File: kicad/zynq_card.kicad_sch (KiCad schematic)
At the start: 0 parts

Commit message: Phase 2: sheet 6 (SoC config): MIO banks, bank 0, boot straps, JTAG
- tools/sheets/06_soc_config.py: U20 units 6/7 (MIO banks 500/501, 1.8 V)
  with every used MIO as a sheet port, boot straps R601-R607 (QSPI boot,
  JTAG cascaded, PLLs on, VMODE 1.8/1.8), PS_POR_B/PS_SRST_B pull-ups,
  PS_MIO_VREF divider; unit 1 (bank 0 at 1.8 V) tied off as on juliancoy,
  R9/R10 kept as block parts, DONE 330R, RSVDGND open (E8)
- J1 (1x5, 3.3 V for FTDI mini-modules) through U601 SN74AVC4T774RSVR,
  the Agilex 3 card's JTAG shifter circuit
- check_block_netlist.py covers sheet 6: on units 1/6/7 only rail/GND balls
  and balls on block-part nets are compared; E3/E7/E8 expected differences;
  J-refs are never block parts (101 parts, 583 pads, 0 failures)
- gen_symbols: SN74AVC4T774 (RSV) box, Conn_01x05; _common: attach(side=),
  pull_r(top=)
- REUSE_LOG E8 and E5/E6 commit refs; ZYNQ_PCB_NOTES JTAG/RSVDGND and the
  UART translator note (needs per-bit direction); STATUS updated

Co-Authored-By: Claude Opus 5.5 <noreply@anthropic.com>
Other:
- sheet 06 soc_config ports: added emmc_rst_n, eth_int_n, eth_rst_n, i2c_scl, i2c_sda, mdc, mdio, ps_clk, ps_por_n, qspi_cs_n, qspi_io0, qspi_io1, qspi_io2, qspi_io3, qspi_sclk, rgmii_rx_ctl, rgmii_rxc, rgmii_rxd0, rgmii_rxd1, rgmii_rxd2, rgmii_rxd3, rgmii_tx_ctl, rgmii_txc, rgmii_txd0, rgmii_txd1, rgmii_txd2, rgmii_txd3, sd_clk, sd_cmd, sd_dat0, sd_dat1, sd_dat2, sd_dat3, uart_rx, uart_tx; removed none

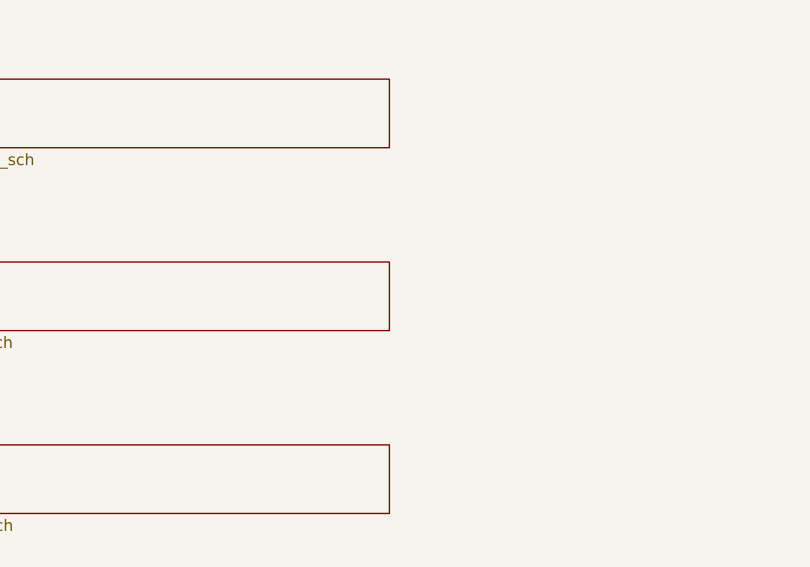
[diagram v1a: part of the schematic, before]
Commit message: Phase 2: sheet 7 (clocks): 33.333 MHz PS_CLK oscillator
- tools/sheets/07_clocks.py: Y701 YXC OT322533.3333MJBA4SL (C2831392,
  1.8 V CMOS, 3225) with the Agilex 3 card's oscillator circuit: EN tied
  to VDD, FB701 BLM18PG121SN1D + C701 470n supply filter, R701 33R
  source-series to the ps_clk port (U20 F7)
- gen_symbols: Oscillator:ASE-xxxMHz
- STATUS updated; REUSE_LOG E8 commit ref

Co-Authored-By: Claude Opus 5.5 <noreply@anthropic.com>
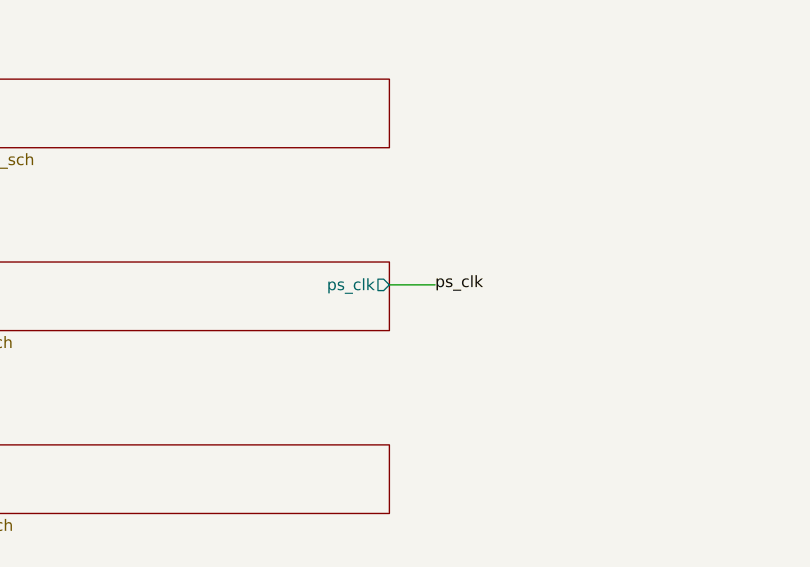
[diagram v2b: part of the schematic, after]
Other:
- sheet 07 clocks ports: added ps_clk; removed none
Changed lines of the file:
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@@
+		)
+	)
+	(label "ps_clk"
+		(at 363.22 53.34 0)
+		(effects
+			(font
+				(size 1.27 1.27)
+			)
+			(justify left)
+		)
+	)
+	(wire
+		(pts
+			(xy 358.14 53.34) (xy 363.22 53.34)
+		)
+		(stroke
+			(width 0)
+			(type default)
 		)
 	)
@@
 			)
 		)
+		(pin "ps_clk" output
+			(at 358.14 53.34 0)
+			(effects
+				(font
+					(size 1.27 1.27)
+				)
+				(justify right)
+			)
+		)

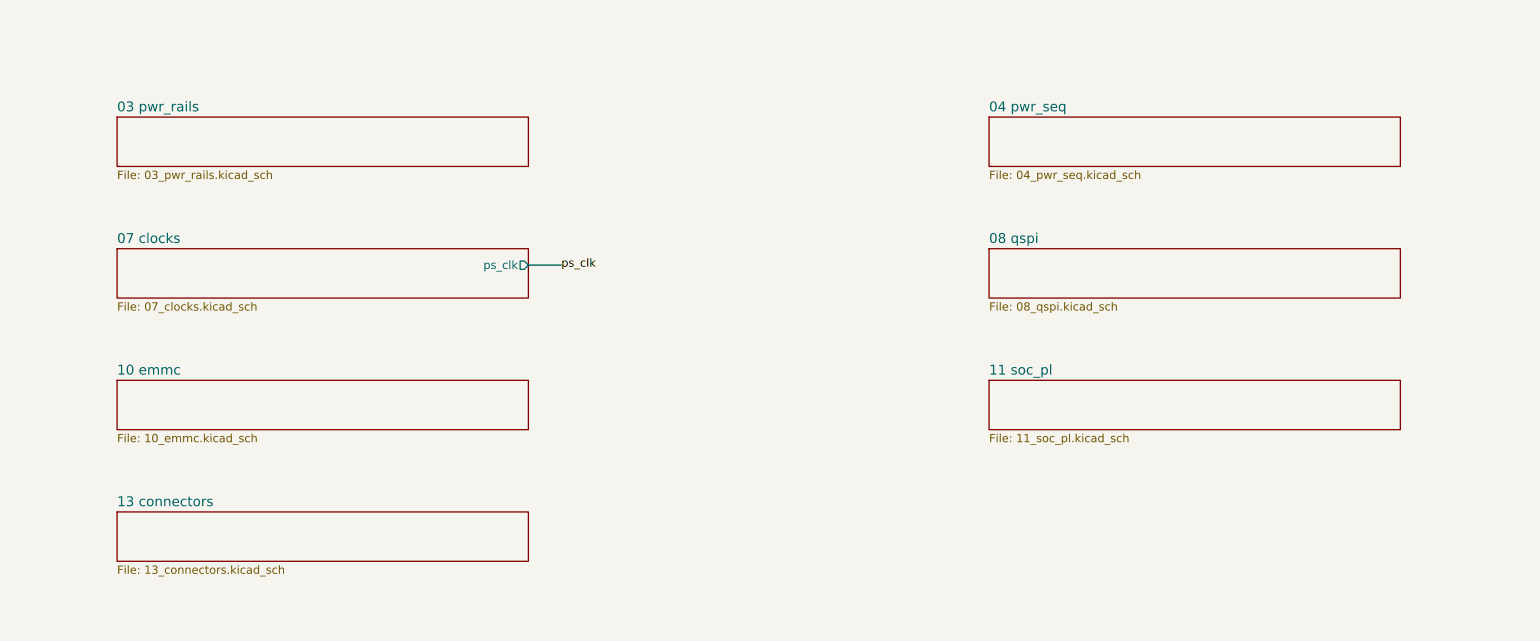
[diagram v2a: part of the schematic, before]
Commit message: Phase 2: sheets 2-4 (power input, rails, sequencing + PS_POR_B supervisor)
Sheet 2: J6 (baseboard J12) to 5V0/GND with PWR_FLAGs and the Ti135 input bulk.
Sheet 3: 4 x TLV62585 (1V0, 1V8, 3V3, 1V35) from the Ti135 cell (_power.py) and
the NCP163 3V3_analog LDO.
Sheet 4: enable chain 1V0 -> 1V8 -> 3V3 + 1V35 -> DDR3_VTT_EN (wired PG AND)
and a TPS3808G01 onto ps_por_n: SENSE on 1V0 (0.895 V), CT = VDD (300 ms),
which keeps PS_POR_B release outside every DS187 Table 23 lockdown window.
Closes the lockdown-window [verify] item. ERC: rails driven; block check 0 failures.

Co-Authored-By: Claude Opus 5.5 <noreply@anthropic.com>
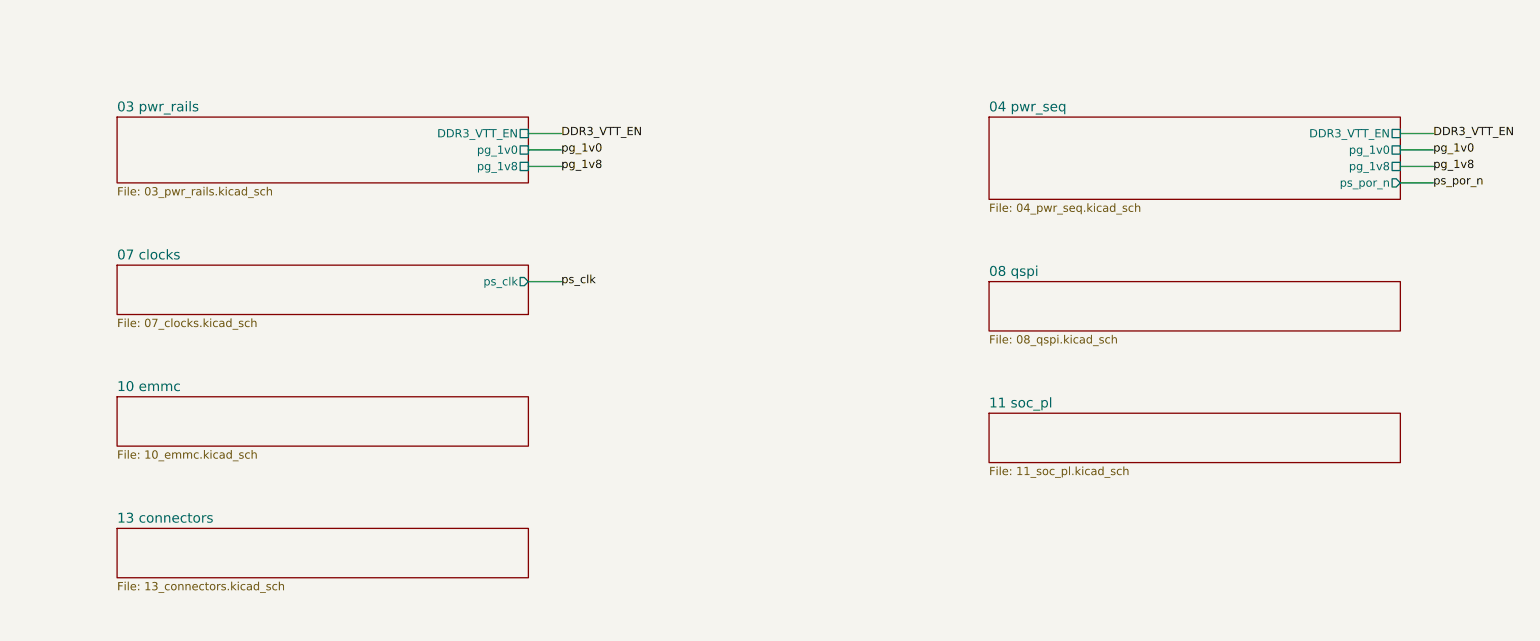
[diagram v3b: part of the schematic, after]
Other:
- sheet 03 pwr_rails ports: added DDR3_VTT_EN, pg_1v0, pg_1v8; removed none
- sheet 04 pwr_seq ports: added DDR3_VTT_EN, pg_1v0, pg_1v8, ps_por_n; removed none
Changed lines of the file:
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@@
+		)
+	)
+	(label "DDR3_VTT_EN"
+		(at 363.22 33.02 0)
+		(effects
+			(font
+				(size 1.27 1.27)
+			)
+			(justify left)
+		)
+	)
+	(wire
+		(pts
+			(xy 358.14 33.02) (xy 363.22 33.02)
+		)
+		(stroke
+			(width 0)
+			(type default)
+		)
+	)
+	(label "pg_1v0"
+		(at 363.22 35.56 0)
+		(effects
+			(font
+				(size 1.27 1.27)
+			)
+			(justify left)
+		)
+	)
+	(wire
+		(pts
+			(xy 358.14 35.56) (xy 363.22 35.56)
+		)
+		(stroke
+			(width 0)
+			(type default)
+		)
+	)
+	(label "pg_1v8"
+		(at 363.22 38.1 0)
+		(effects
+			(font
+				(size 1.27 1.27)
+			)
+			(justify left)
+		)
+	)
+	(wire
+		(pts
+			(xy 358.14 38.1) (xy 363.22 38.1)
+		)
+		(stroke
+			(width 0)
+			(type default)
+		)
+	)
+	(label "DDR3_VTT_EN"
+		(at 497.84 33.02 0)
+		(effects
+			(font
+				(size 1.27 1.27)
+			)
+			(justify left)
+		)
+	)
+	(wire
+		(pts
+			(xy 492.76 33.02) (xy 497.84 33.02)
+		)
+		(stroke
+			(width 0)
+			(type default)
+		)
+	)
+	(label "pg_1v0"
+		(at 497.84 35.56 0)
+		(effects
+			(font
+				(size 1.27 1.27)
+			)
+			(justify left)
+		)
+	)
+	(wire
+		(pts
+			(xy 492.76 35.56) (xy 497.84 35.56)
+		)
+		(stroke
+			(width 0)
+			(type default)
+		)
+	)
+	(label "pg_1v8"
+		(at 497.84 38.1 0)
+		(effects
+			(font
+				(size 1.27 1.27)
+			)
+			(justify left)
+		)
+	)
+	(wire
+		(pts
+			(xy 492.76 38.1) (xy 497.84 38.1)
+		)
+		(stroke
+			(width 0)
+			(type default)
+		)
+	)
+	(label "ps_por_n"
+		(at 497.84 40.64 0)
+		(effects
+			(font
+				(size 1.27 1.27)
+			)
+			(justify left)
+		)
+	)
+	(wire
+		(pts
+			(xy 492.76 40.64) (xy 497.84 40.64)
+		)
+		(stroke
+			(width 0)
+			(type default)
 		)
 	)
@@
 	)
 	(label "ps_clk"
-		(at 363.22 53.34 0)
-		(effects
-			(font
-				(size 1.27 1.27)
-			)
-			(justify left)
-		)
-	)
-	(wire
-		(pts
-			(xy 358.14 53.34) (xy 363.22 53.34)
+		(at 363.22 55.88 0)
+		(effects
+			(font
+				(size 1.27 1.27)
+			)
+			(justify left)
+		)
+	)
+	(wire
+		(pts
+			(xy 358.14 55.88) (xy 363.22 55.88)
 		)
 		(stroke
@@
 	(sheet
 		(at 294.64 30.48)
-		(size 63.5 7.62)
+		(size 63.5 10.16)
 		(exclude_from_sim no)
 		(in_bom yes)
@@
 		)
 		(property "Sheetfile" "03_pwr_rails.kicad_sch"
-			(at 294.64 38.7 0)
+			(at 294.64 41.24 0)
 			(effects
 				(font
@@
 			)
 		)
+		(pin "DDR3_VTT_EN" passive
+			(at 358.14 33.02 0)
+			(effects
+				(font
+					(size 1.27 1.27)
+				)
+				(justify right)
+			)
+		)
+		(pin "pg_1v0" passive
+			(at 358.14 35.56 0)
+			(effects
+				(font
+					(size 1.27 1.27)
+				)
+				(justify right)
+			)
+		)
+		(pin "pg_1v8" passive
+			(at 358.14 38.1 0)
+			(effects
+				(font
+					(size 1.27 1.27)
+				)
+				(justify right)
+			)
+		)
 	)
 	(sheet
 		(at 429.26 30.48)
-		(size 63.5 7.62)
+		(size 63.5 12.7)
 		(exclude_from_sim no)
 		(in_bom yes)
@@
 		)
 		(property "Sheetfile" "04_pwr_seq.kicad_sch"
-			(at 429.26 38.7 0)
+			(at 429.26 43.78 0)
 			(effects
 				(font
@@
 					(page "5")
 				)
+			)
+		)
+		(pin "DDR3_VTT_EN" passive
+			(at 492.76 33.02 0)
+			(effects
+				(font
+					(size 1.27 1.27)
+				)
+				(justify right)
+			)
+		)
+		(pin "pg_1v0" passive
+			(at 492.76 35.56 0)
+			(effects
+				(font
+					(size 1.27 1.27)
+				)
+				(justify right)
+			)
+		)
+		(pin "pg_1v8" passive
+			(at 492.76 38.1 0)
+			(effects
+				(font
+					(size 1.27 1.27)
+				)
+				(justify right)
+			)
+		)
+		(pin "ps_por_n" output
+			(at 492.76 40.64 0)
+			(effects
+				(font
+					(size 1.27 1.27)
+				)
+				(justify right)
 			)
 		)
@@
 	)
 	(sheet
-		(at 294.64 50.8)
+		(at 294.64 53.34)
 		(size 63.5 7.62)
 		(exclude_from_sim no)
@@
 		)
 		(property "Sheetname" "07 clocks"
-			(at 294.64 50.1 0)
+			(at 294.64 52.64 0)
 			(effects
 				(font
@@
 		)
 		(property "Sheetfile" "07_clocks.kicad_sch"
-			(at 294.64 59.02 0)
+			(at 294.64 61.56 0)
 			(effects
 				(font
@@
 		)
 		(pin "ps_clk" output
-			(at 358.14 53.34 0)
+			(at 358.14 55.88 0)
 			(effects
 				(font
@@
 	)
 	(sheet
-		(at 429.26 50.8)
+		(at 429.26 55.88)
 		(size 63.5 7.62)
 		(exclude_from_sim no)
@@
 		)
 		(property "Sheetname" "08 qspi"
-			(at 429.26 50.1 0)
+			(at 429.26 55.18 0)
 			(effects
 				(font
@@
 		)
 		(property "Sheetfile" "08_qspi.kicad_sch"
-			(at 429.26 59.02 0)
+			(at 429.26 64.1 0)
 			(effects
 				(font
@@
 	)
 	(sheet
-		(at 294.64 71.12)
+		(at 294.64 73.66)
 		(size 63.5 7.62)
 		(exclude_from_sim no)
@@
 		)
 		(property "Sheetname" "10 emmc"
-			(at 294.64 70.42 0)
+			(at 294.64 72.96 0)
 			(effects
 				(font
@@
 		)
 		(property "Sheetfile" "10_emmc.kicad_sch"
-			(at 294.64 79.34 0)
+			(at 294.64 81.88 0)
 			(effects
 				(font
@@
 	)
 	(sheet
-		(at 429.26 71.12)
+		(at 429.26 76.2)
 		(size 63.5 7.62)
 		(exclude_from_sim no)
@@
 		)
 		(property "Sheetname" "11 soc_pl"
-			(at 429.26 70.42 0)
+			(at 429.26 75.5 0)
 			(effects
 				(font
@@
 		)
 		(property "Sheetfile" "11_soc_pl.kicad_sch"
-			(at 429.26 79.34 0)
+			(at 429.26 84.42 0)
 			(effects
 				(font
@@
 	)
 	(sheet
-		(at 294.64 91.44)
+		(at 294.64 93.98)
 		(size 63.5 7.62)
 		(exclude_from_sim no)
@@
 		)
 		(property "Sheetname" "13 connectors"
-			(at 294.64 90.74 0)
+			(at 294.64 93.28 0)
 			(effects
 				(font
@@
 		)
 		(property "Sheetfile" "13_connectors.kicad_sch"
-			(at 294.64 99.66 0)
-			(effects
-				(font
+			(at 294.64 102.2 0)
+			(effects
+				(font

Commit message: Phase 2: sheets 8-10 (QSPI flash, RTL8211F Ethernet, eMMC)
Sheet 8: IS25WP128-RHLE on QSPI0 at 1V8, CS# pull-up, RESET# on ps_por_n.
Sheet 9: the Ti135 RTL8211FDI-CG + HR911130A sheet on GEM0 RGMII / MDIO0.
RGMII and MDIO pads at 1.8 V via the PHY's internal LDO; INTB is open drain,
so its 1V8 pull-up is fine (closes the INTB [verify]). eth_rst_n pull-down
is 1k to beat the MIO reset pull-up.
Sheet 10: THGAMVG7T13BAIL on SD0, 4-bit, with the KIOXIA decoupling values.
Symbols ported from the Ti135 card into gen_symbols.py; its flash and RJ45
footprints copied into lib/zynq_card.pretty. fill_footprints() in _common.py.
Every port checked against the U20 MIO balls in the netlist. ERC: only the
UART/I2C ports and the PL bank units remain; block check 0 failures.

Co-Authored-By: Claude Opus 5.5 <noreply@anthropic.com>
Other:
- sheet 08 qspi ports: added ps_por_n, qspi_cs_n, qspi_io0, qspi_io1, qspi_io2, qspi_io3, qspi_sclk; removed none
- sheet 09 ethernet ports: added eth_int_n, eth_rst_n, mdc, mdio, rgmii_rx_ctl, rgmii_rxc, rgmii_rxd0, rgmii_rxd1, rgmii_rxd2, rgmii_rxd3, rgmii_tx_ctl, rgmii_txc, rgmii_txd0, rgmii_txd1, rgmii_txd2, rgmii_txd3; removed none
- sheet 10 emmc ports: added emmc_rst_n, sd_clk, sd_cmd, sd_dat0, sd_dat1, sd_dat2, sd_dat3; removed none

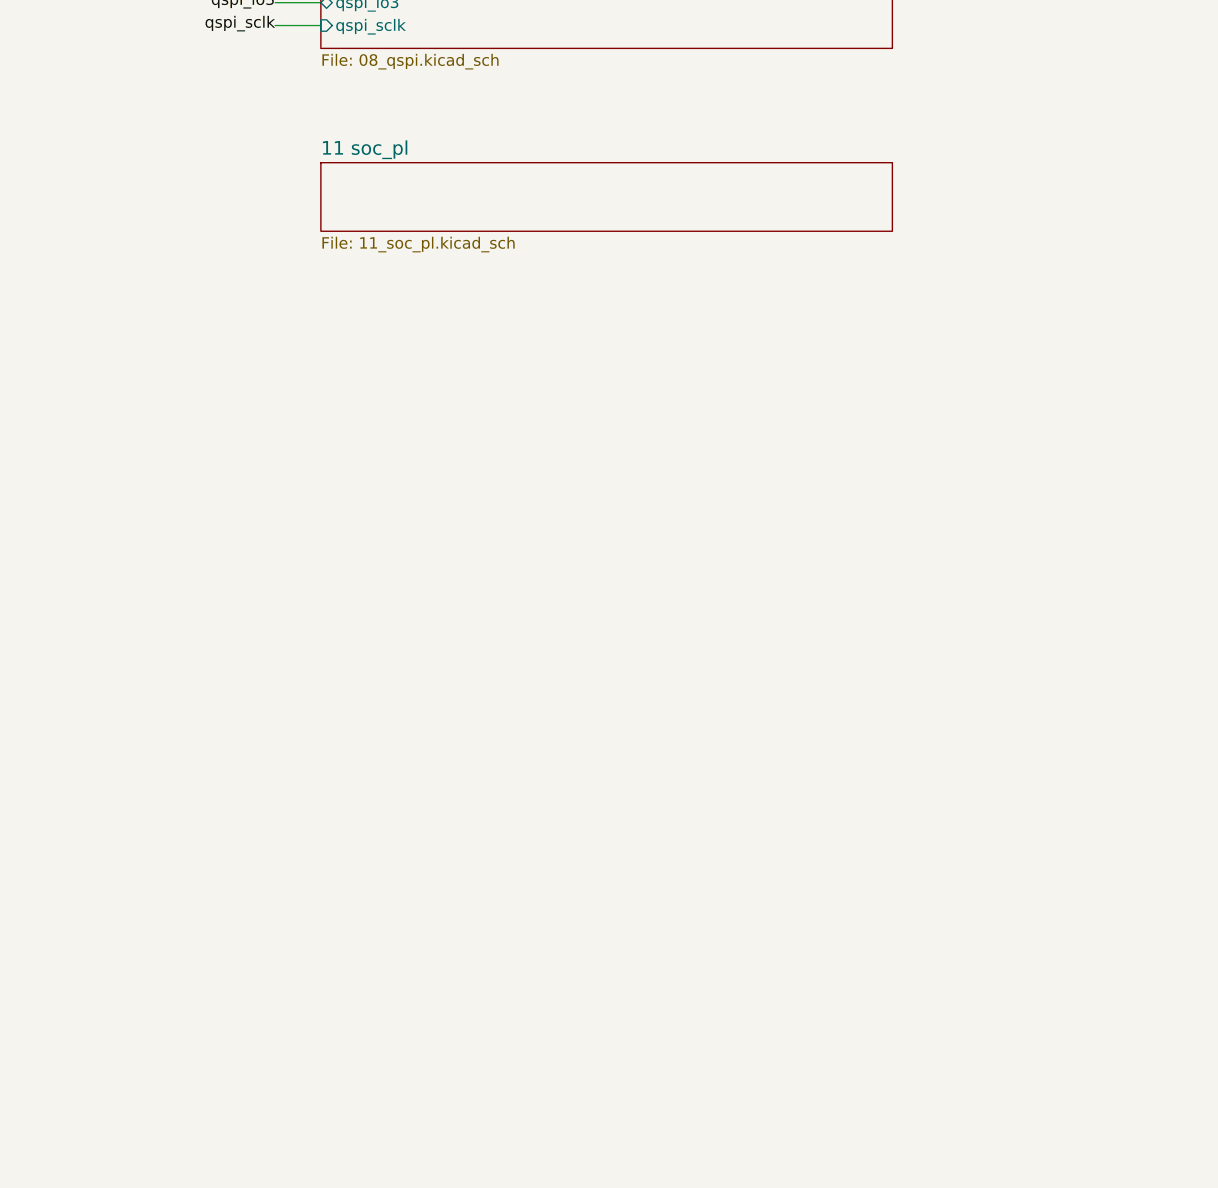
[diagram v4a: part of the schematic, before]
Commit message: Phase 2: sheet 11 (PL banks 13/33/34/35, all VCCO on 3V3)
U20 units 2-5 with one hierarchical label per pin-plan signal (ball and
pin function asserted against the symbol); unused balls left open.
PUDC_B (K16) tied to VCCO_34; user LEDs D1101/D1102 on bank 33.
New block change E9: juliancoy grounds every I/O ball of banks 34/35;
here they carry our nets or stay open (copper planned). The block check
covers sheet 11, with E7/E9 balls generated from the symbol: 0 failures,
322 U20 balls. All 52 pin-plan signals verified on their balls.

Co-Authored-By: Claude Opus 5.5 <noreply@anthropic.com>
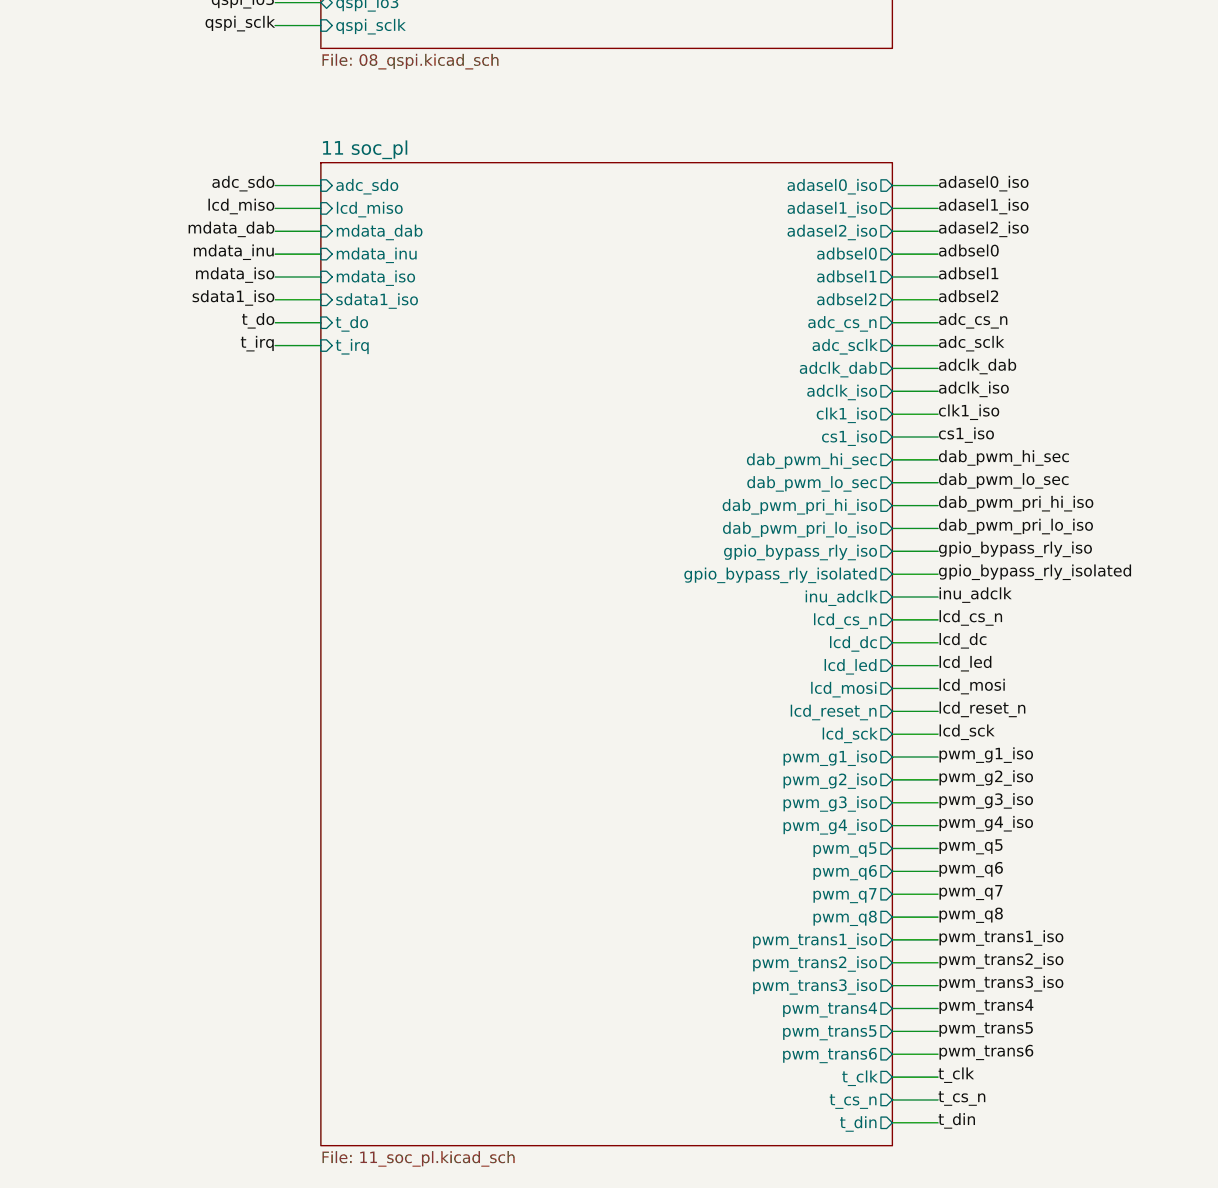
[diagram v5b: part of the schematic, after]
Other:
- sheet 11 soc_pl ports: added adasel0_iso, adasel1_iso, adasel2_iso, adbsel0, adbsel1, adbsel2, adc_cs_n, adc_sclk, adc_sdo, adclk_dab, adclk_iso, clk1_iso, cs1_iso, dab_pwm_hi_sec, dab_pwm_lo_sec, dab_pwm_pri_hi_iso, dab_pwm_pri_lo_iso, gpio_bypass_rly_iso, gpio_bypass_rly_isolated, inu_adclk, lcd_cs_n, lcd_dc, lcd_led, lcd_miso, lcd_mosi, lcd_reset_n, lcd_sck, mdata_dab, mdata_inu, mdata_iso, pwm_g1_iso, pwm_g2_iso, pwm_g3_iso, pwm_g4_iso, pwm_q5, pwm_q6, pwm_q7, pwm_q8, pwm_trans1_iso, pwm_trans2_iso, pwm_trans3_iso, pwm_trans4, pwm_trans5, pwm_trans6, sdata1_iso, t_clk, t_cs_n, t_din, t_do, t_irq; removed none
